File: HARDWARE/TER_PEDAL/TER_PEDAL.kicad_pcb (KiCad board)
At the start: 4 copper layers, 78.2 x 40 mm, 56 parts, among them J1 DEBUG, J2 APPS_1, J3 RJ45_Shielded, J4 APPS_2, J5 BPPS_1, J6 SteerSensor, SW1 RST, U1 STM32F103C8Tx, U2 TSR_1-2450, U3 LM1117MP-3.3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

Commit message: Rearranged board
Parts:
- Y1: footprint Crystal:Crystal_HC52-6mm_Vertical -> Crystal:Crystal_SMD_5032-2Pin_5.0x3.2mm
- moved J6 34.7 mm to (117.6, 105.8)
- moved C13 32.2 mm to (177.2, 108.0), turned to -90 degrees
- moved G*** 31.5 mm to (119.2, 70.5)
- moved U3 26.3 mm to (172.0, 107.0), turned to 180 degrees
- moved C12 25.5 mm to (177.2, 105.0), turned to -90 degrees
- moved C14 22.9 mm to (122.7, 84.8)
- moved R7 22.9 mm to (122.7, 81.2)
- moved SW1 22.9 mm to (119.8, 83.0)
- moved R10 15.9 mm to (147.5, 101.2)
- moved J4 15.2 mm to (145.1, 105.4)
- moved J2 14.3 mm to (132.6, 105.8)
- moved JP1 13.5 mm to (160.4, 82.0)
- moved JP2 13.5 mm to (160.4, 85.0)
- moved R4 13.5 mm to (157.9, 79.5)
- moved R5 13.5 mm to (157.7, 87.2)
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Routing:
- net Net-(C16-Pad1): track 10.4 -> 5.55 mm
- net /SENSORS/SENS_2: track 3.23 -> 0.00 mm
- net /MICRO/OSC_IN: track 9.99 -> 11.8 mm
- net +5V: track 3.47 -> 2.94 mm
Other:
- outline, holes or cut-outs redrawn

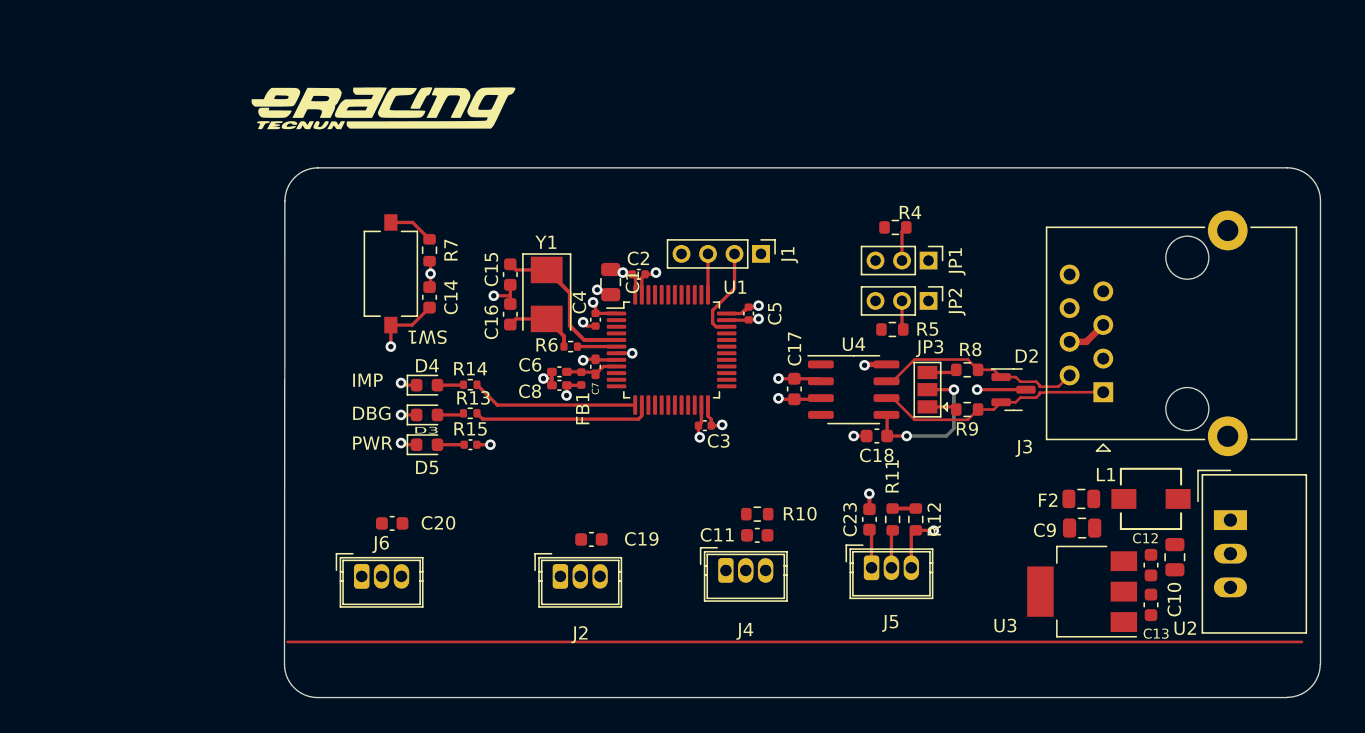
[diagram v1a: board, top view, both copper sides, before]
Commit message: Added holes, connectors and finished re-layout
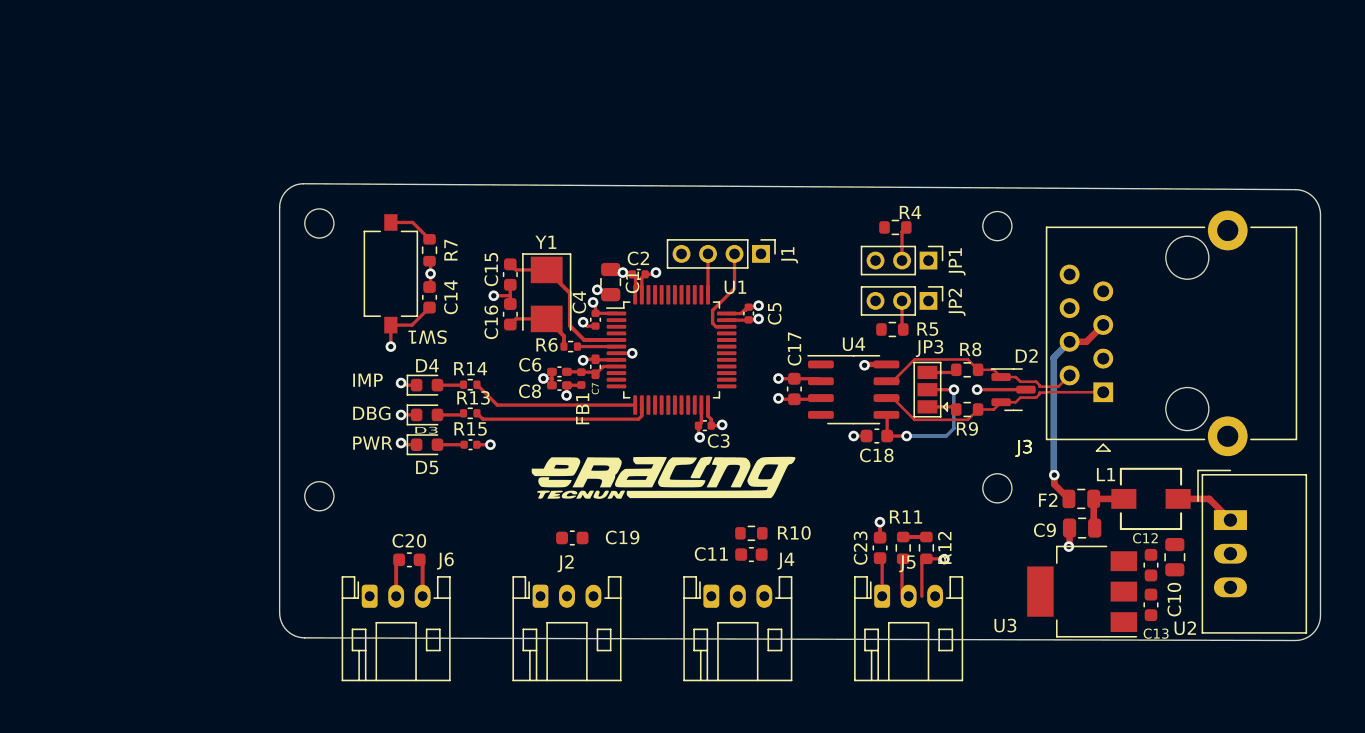
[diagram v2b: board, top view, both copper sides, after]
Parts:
- added H1: MountingHole, MountingHole:MountingHole_2.2mm_M2, F.Cu at (114.4, 79.2)
- added H2: MountingHole, MountingHole:MountingHole_2.2mm_M2, F.Cu at (114.4, 99.8)
- added H3: MountingHole, MountingHole:MountingHole_2.2mm_M2, F.Cu at (165.6, 99.2)
- added H4: MountingHole, MountingHole:MountingHole_2.2mm_M2, F.Cu at (165.6, 79.4)
- J2, J4, J5, J6: footprint Connector_Wuerth:Wuerth_WR-WTB_64800311622_1x03_P1.50mm_Vertical -> Connector_JST:JST_PH_S3B-PH-K_1x03_P2.00mm_Horizontal
- moved G*** 35.0 mm to (140.4, 98.4)
- moved C20 3.04 mm to (121.2, 104.6)
- moved C23 2.29 mm to (156.7, 103.7)
- moved R11 2.29 mm to (158.5, 103.7)
- moved R12 2.29 mm to (160.2, 103.7)
- moved J5 2.29 mm to (156.9, 107.3)
- moved J4 2.24 mm to (144.0, 107.3)
- moved J2 2.12 mm to (131.1, 107.3)
- moved J6 1.62 mm to (118.2, 107.3)
- moved C11 1.52 mm to (147.0, 104.2)
- moved R10 1.52 mm to (147.0, 102.6)
- moved C19 1.45 mm to (133.5, 103.0)
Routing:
- net +24V: track 3.07 -> 15.9 mm, vias 0 -> 1
- net Net-(U2-Vin): track 0.00 -> 4.61 mm
- net Net-(C9-Pad1): track 0.00 -> 4.51 mm
- net GND: track 40.5 -> 44.8 mm, vias 18 -> 19
- net /MICRO/STEER_ADC: track 0.00 -> 2.84 mm
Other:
- board size 78.2 x 40 mm -> 78.6 x 34.5 mm

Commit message: Finished Routing for redisign
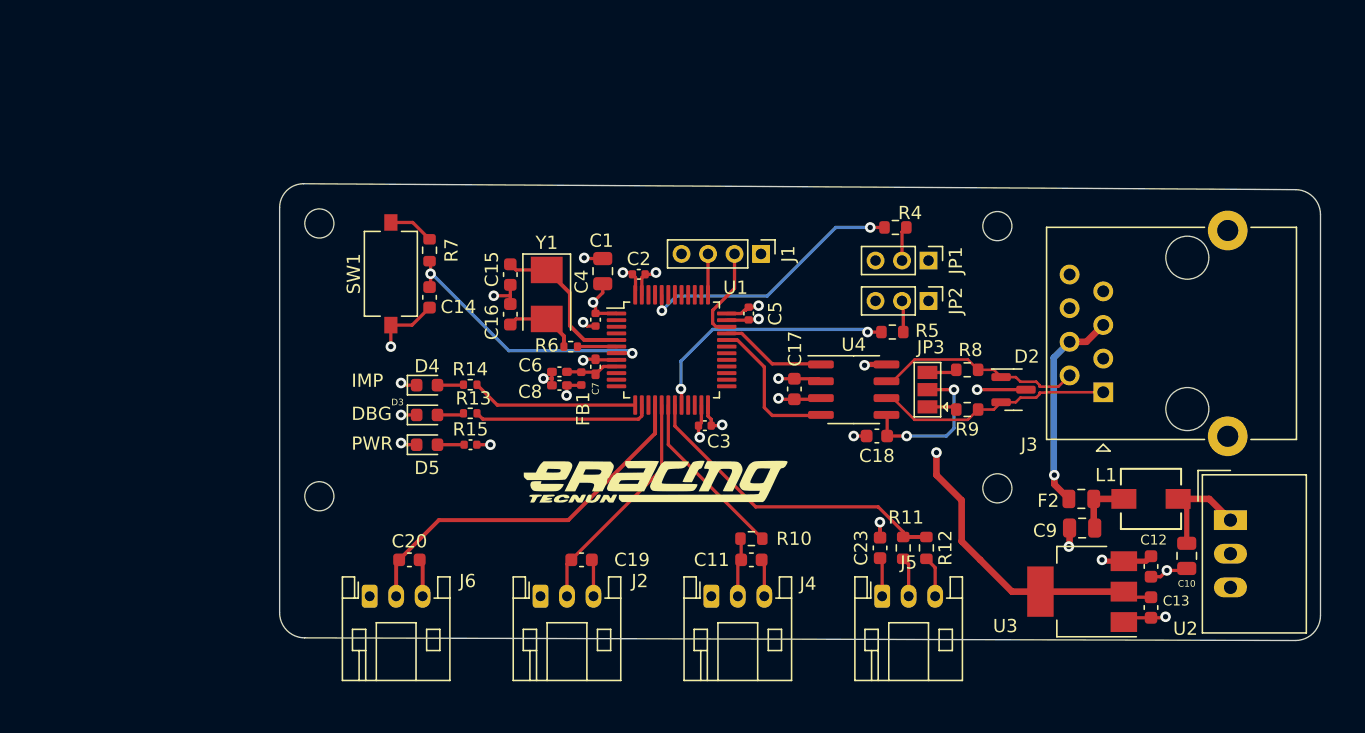
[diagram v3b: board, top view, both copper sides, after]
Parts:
- moved C19 1.79 mm to (134.2, 104.6)
- moved C1 1.02 mm to (135.8, 82.8), turned to 90 degrees
- moved C10 0.91 mm to (179.9, 104.3)
- moved G*** 0.67 mm to (139.8, 98.7)
- moved R10 0.40 mm to (147.0, 103.0)
- moved C11 0.40 mm to (147.0, 104.6)
- moved C13 0.20 mm to (177.2, 108.2)
- moved R5 0.19 mm to (157.7, 87.4)
- moved C12 0.10 mm to (177.2, 105.1)
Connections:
- U1 pad 16: /SENSORS/SENS_1 -> /MICRO/STEER_ADC
- U1 pad 17: /MICRO/APPS_2_ADC -> /SENSORS/SENS_1
- U1 pad 18: /MICRO/STEER_ADC -> /MICRO/APPS_2_ADC
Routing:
- net /MICRO/STEER_ADC: track 2.84 -> 28.3 mm
- net +3.3V: track 16.9 -> 41.2 mm, vias 7 -> 8
- net /MICRO/BPPS_ADC: track 1.75 -> 24.3 mm
- net /MICRO/BOOT0: track 0.00 -> 20.6 mm, vias 0 -> 2
- net /MICRO/BOOT1: track 0.04 -> 19.6 mm, vias 0 -> 2
- net /MICRO/NRST: track 3.21 -> 20.9 mm
- net /SENSORS/SENS_1: track 0.00 -> 17.4 mm
- net /MICRO/APPS_2_ADC: track 0.00 -> 13.0 mm
- net /CAN/CAN_RX: track 0.00 -> 11.3 mm
- net GND: track 44.8 -> 55.8 mm, vias 19 -> 20
- net /CAN/CAN_TX: track 0.00 -> 8.08 mm
- net /SENSORS/SENS_2: track 0.00 -> 4.47 mm
- net +5V: track 2.94 -> 6.84 mm, vias 0 -> 1
- net Net-(U2-Vin): track 4.61 -> 8.23 mm
- net /CAN/CAN-: track 18.9 -> 18.0 mm
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
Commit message: Added Labels on silkscreen and, versioning and IMG
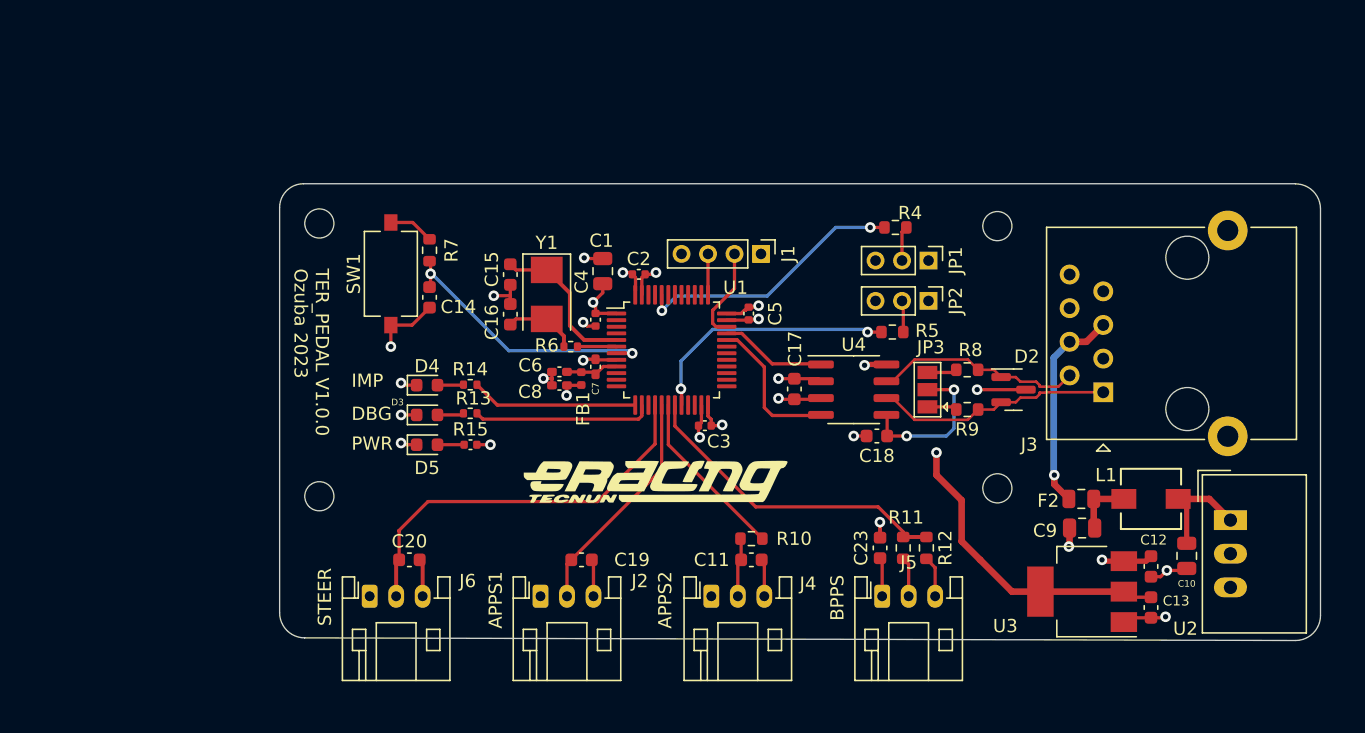
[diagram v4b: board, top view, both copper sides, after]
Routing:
- net /MICRO/STEER_ADC: track 28.3 -> 30.1 mm
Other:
- outline, holes or cut-outs redrawn
- board text added: "APPS1"
- board text added: "APPS2"
- board text added: "BPPS"
- board text added: "STEER"
- board text added: "TER_PEDAL V1.0.0 Ozuba 2023"
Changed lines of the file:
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@@
   (gr_arc (start 111.4 78) (mid 111.927208 76.727208) (end 113.2 76.2)
     (stroke (width 0.1) (type default)) (layer "Edge.Cuts"))
-  (gr_line (start 113.2 76.2) (end 188.107912 76.64582)
+  (gr_line (start 113.2 76.2) (end 188.107912 76.2)
     (stroke (width 0.1) (type default)) (layer "Edge.Cuts"))
   (gr_line (start 188.107912 110.692088) (end 113.292088 110.492088)
     (stroke (width 0.1) (type default)) (layer "Edge.Cuts"))
-  (gr_line (start 190 78.537908) (end 190 108.8)
+  (gr_line (start 190 78.1) (end 190 108.8)
     (stroke (width 0.1) (type default)) (layer "Edge.Cuts"))
   (gr_arc (start 113.292088 110.492088) (mid 111.95418 109.937908) (end 111.4 108.6)
@@
   (gr_arc (start 190 108.8) (mid 189.44582 110.137908) (end 188.107912 110.692088)
     (stroke (width 0.1) (type default)) (layer "Edge.Cuts"))
-  (gr_arc (start 188.107912 76.64582) (mid 189.44582 77.2) (end 190 78.537908)
+  (gr_arc (start 188.107912 76.207912) (mid 189.44581 76.762096) (end 190 78.1)
     (stroke (width 0.1) (type default)) (layer "Edge.Cuts"))
   (gr_text "PWR\n" (at 116.82 96.408) (layer "F.SilkS")
@@
   )
   (gr_text "DBG" (at 116.82 94.158) (layer "F.SilkS")
+    (effects (font (size 1 1) (thickness 0.15)) (justify left bottom))
+  )
+  (gr_text "APPS1" (at 128.3 109.8 90) (layer "F.SilkS")
+    (effects (font (size 1 1) (thickness 0.15)) (justify left bottom))
+  )
+  (gr_text "STEER" (at 115.4 109.6 90) (layer "F.SilkS")
+    (effects (font (size 1 1) (thickness 0.15)) (justify left bottom))
+  )
+  (gr_text "TER_PEDAL V1.0.0\nOzuba 2023" (at 112.4 82.6 270) (layer "F.SilkS")
+    (effects (font (size 1 1) (thickness 0.15)) (justify left bottom))
+  )
+  (gr_text "APPS2" (at 141.1 109.8 90) (layer "F.SilkS")
+    (effects (font (size 1 1) (thickness 0.15)) (justify left bottom))
+  )
+  (gr_text "BPPS" (at 154.1 109.2 90) (layer "F.SilkS")
     (effects (font (size 1 1) (thickness 0.15)) (justify left bottom))
   )
@@
   (segment (start 158.75 95.25) (end 161.75 95.25) (width 0.25) (layer "B.Cu") (net 8))
   (segment (start 162.32 94.68) (end 162.32 91.75) (width 0.25) (layer "B.Cu") (net 8))
-  (segment (start 133.2 101.6) (end 139.75 95.05) (width 0.3) (layer "F.Cu") (net 9))
   (segment (start 120.2 107.35) (end 120.2 104.825) (width 0.3) (layer "F.Cu") (net 9))
-  (segment (start 120.425 104.6) (end 123.425 101.6) (width 0.3) (layer "F.Cu") (net 9))
+  (segment (start 139.75 92.9125) (end 139.75 95.85) (width 0.25) (layer "F.Cu") (net 9))
   (segment (start 120.2 104.825) (end 120.425 104.6) (width 0.3) (layer "F.Cu") (net 9))
-  (segment (start 123.425 101.6) (end 133.2 101.6) (width 0.3) (layer "F.Cu") (net 9))
-  (segment (start 139.75 95.05) (end 139.75 92.9125) (width 0.3) (layer "F.Cu") (net 9))
+  (segment (start 135.4 100.2) (end 122.6 100.2) (width 0.25) (layer "F.Cu") (net 9))
+  (segment (start 120.4 102.4) (end 120.425 102.425) (width 0.25) (layer "F.Cu") (net 9))
+  (segment (start 139.75 95.85) (end 135.4 100.2) (width 0.25) (layer "F.Cu") (net 9))
+  (segment (start 122.6 100.2) (end 120.4 102.4) (width 0.25) (layer "F.Cu") (net 9))
+  (segment (start 120.425 102.425) (end 120.425 104.6) (width 0.25) (layer "F.Cu") (net 9))
   (segment (start 167.338751 91.15) (end 168.531396 91.15) (width 0.2) (layer "F.Cu") (net 11))
   (segment (start 170.205 91.525) (end 171.055 90.675) (width 0.2) (layer "F.Cu") (net 11))
@@
     (polygon
       (pts
-        (xy 111.45 110.6)
-        (xy 190 110.8)
-        (xy 190 76.7)
-        (xy 111.45 76.3)
+        (xy 111.45 110.5)
+        (xy 190 110.7)
+        (xy 190 76.2)
+        (xy 111.5 76.2)
       )
     )
@@
     (polygon
       (pts
-        (xy 111.449998 76.500991)
+        (xy 111.5 76.2)
         (xy 111.449998 110.5)
         (xy 141.5 110.6)
@@
         (xy 154 97.412032)
         (xy 168.749998 97.293445)
-        (xy 168.749998 76.600991)
+        (xy 168.8 76.2)
       )
     )

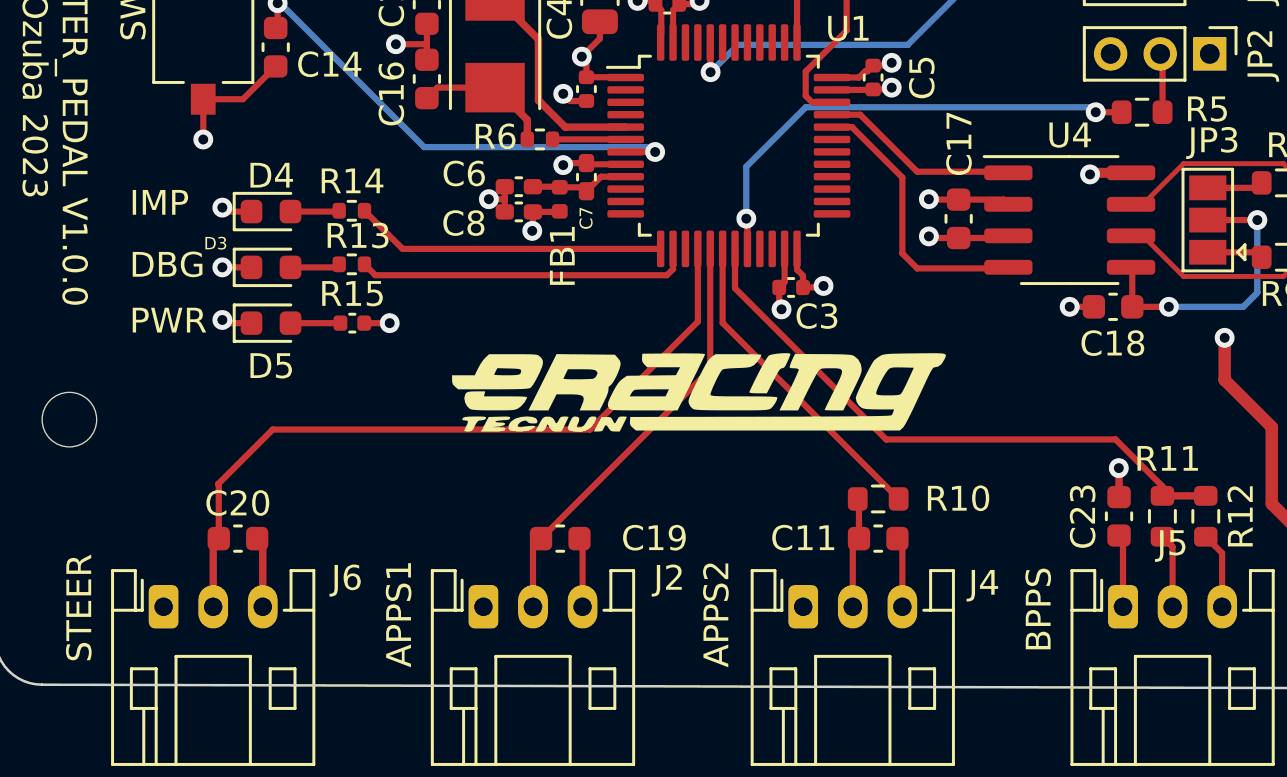
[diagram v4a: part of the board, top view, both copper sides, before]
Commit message: Fixed ferrite bead imposible size to 805
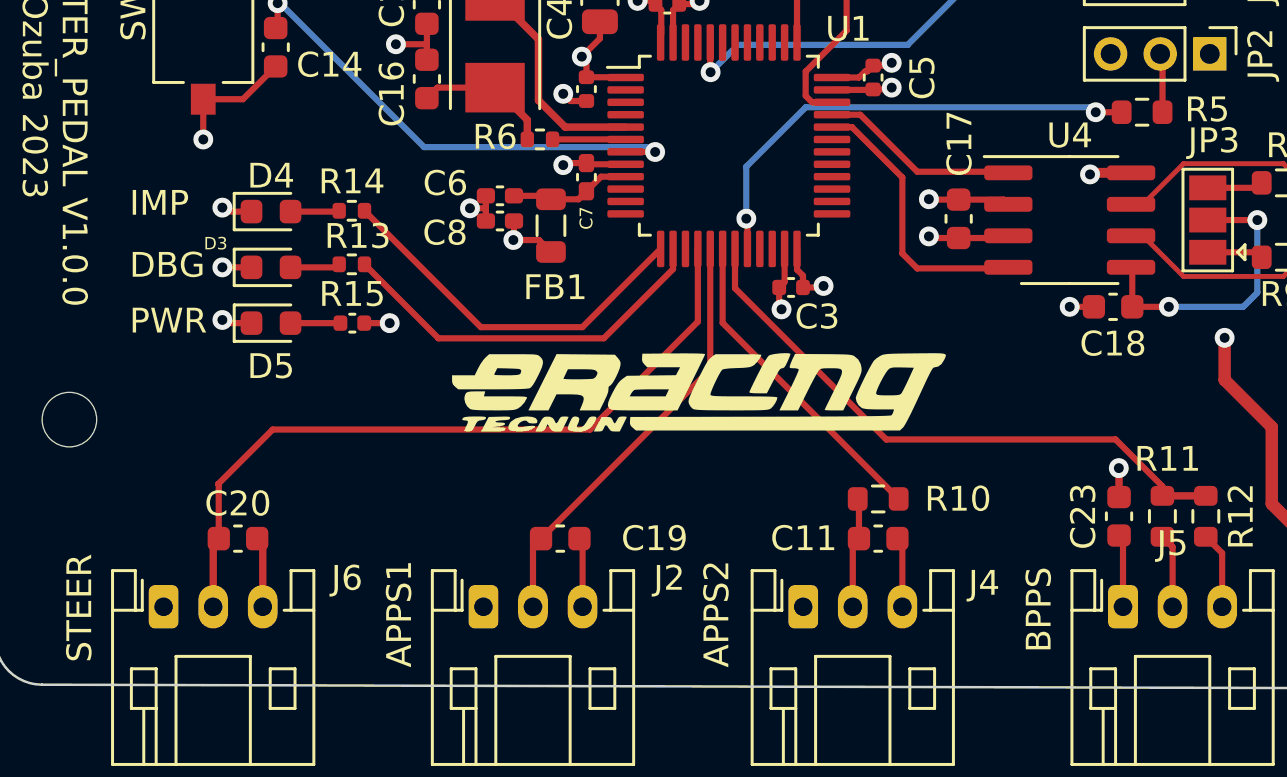
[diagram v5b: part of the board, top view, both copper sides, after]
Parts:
- FB1: footprint Inductor_SMD:L_0402_1005Metric -> Inductor_SMD:L_0805_2012Metric
- moved FB1 1.12 mm to (133.8, 92.0)
- moved C6 0.85 mm to (131.8, 90.8)
- moved C8 0.85 mm to (131.8, 91.8)
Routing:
- net /IMP_LED: track 12.6 -> 15.2 mm
- net /DBG_LED: track 13.5 -> 15.7 mm
- net +3.3VADC: track 4.06 -> 4.94 mm
- net +3.3V: track 41.2 -> 41.8 mm
